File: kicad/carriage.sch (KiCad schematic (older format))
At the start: 21 parts, among them P10 \"1791-ZL262-8SG\", P11 \"1791-ZL262-8SG\", P12 \"1791-ZL262-8SG\", P13 \"1791-ZL262-8SG\", P8 \"1791-ZL262-8SG\", P9 \"1791-ZL262-8SG\", Q1 IRLR2905ZPBF, U1 \"1815-CD40109BPWR\"

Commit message: Draw schematic
Added sheet for panel connector and sheet for Y axis circuits.
Added ULN2803

References: #1 #11 #7 #5
Close #13
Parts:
- removed P10: \"1791-ZL262-8SG\", 7408hacks/dibfv, symbol "1791-ZL262-8SG"
- removed unit 3 of U1
- removed unit 4 of U1
- removed unit 5 of U1
- added C? (x2): 4u7/10V, 0805, symbol C
- added C?: \"1795-EEEFK1V101XP\", 7408hacks/dnxpf, symbol "1795-EEEFK1V101XP"
- added D? (x2): RED, 0805, symbol LED
- added JP?: \"1797-61300621121\", 7408hacks/dnxpn, symbol "1797-61300621121"
- added P9, P? (x2): \"1791-ZL262-8SG\", 7408hacks/dibfv, symbol "1791-ZL262-8SG"
- added Q2: IRLR2905ZPBF, D-PAK, symbol IRLR2905ZPBF
- added R7, R8, R? (x2): 22k, 0603, symbol R
- added R9: 10R, 0603, symbol R
- added R? (x4): 4k7 1%, 0603, symbol R
- added U?: \"1762-ULN2803ADW\", Plecharts/axkx7, symbol "1762-ULN2803ADW"
- R1, R2, R3, R4, R5, R6: value 10k -> 22k
- R10: renamed from R7; value 10k -> 10R
- renumbered P9 to P10
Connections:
- net labels added: A13, A14, A8, D46, D48, D9
- wire segments 96 -> 142
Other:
- note added: "Z"
- moved on the sheet: R10

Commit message: Draw schematic
Commit before trying newer version of KiCad
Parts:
- gave numbers to parts that had none: 15

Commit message: Draw schematic
Finished redrawing basic RAMPS schematic

References: #1 #4 #7 #15
Close #5 #17 #18
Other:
- note added: "Standard 40W heater @12V - 3.4A\n40W heater @24V - 1.7A"
- note added: "Standard IDC 2.54mm:\n- curent rating 2-3A\n- contact resistance max. 20mOhm\n\nStandard ribbon cable 1.27mm pitch, 28AWG (0.08mm2):\n- current rating 1A (dT=10*C)\n- resistance 0,24Ohm/m\n\nThere is also thicker 26AWG (0.13mm2) version.\n"
- moved on the sheet: R7, R8

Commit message: Change components to my own
References: #1 #19
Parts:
- removed C1, C2, C3, C8: \"1795-EEEFK1V101XP\", 7408hacks/dnxpf, symbol "1795-EEEFK1V101XP"
- removed C9: 4u7/10V, 0805, symbol C
- removed R1, R17, R18, R2, R4, R5: 22k, 0603, symbol R
- removed R21: 4k7 1%, 0603, symbol R
- added C7: 4u7/10V, 0805, symbol C
- added C? (x4): 100u/35V, symbol Cpol
- added R11: 4k7 1%, 0603, symbol R
- added R13: 10R, 0603, symbol R
- added R14, R15, R16, R3, R9: 22k, 0603, symbol R
- R10: value 10R -> 22k
- renumbered C10 to C4, D3 to D6, D2 to D7, JP2 to JP1, JP1 to JP2, JP5 to JP3, JP3 to JP4, P9 to P2, P11 to P3, P8 to P4, P10 to P5, P16 to P6, P17 to P7, P12 to P8, P13 to P9, R20 to R1, R19 to R12, R3 to R2, R22 to R4, R9 to R5
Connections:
- wire segments 142 -> 144
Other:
- moved on the sheet: C4, R1, R12, R2, R4, R5

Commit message: Add YZ connector. Add endstop filters.
Close #23
References: #3 #20
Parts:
- removed C? (x3): 100u/35V, symbol Cpol
- removed JP1, JP2, JP3, JP4: \"1797-61300621121\", 7408hacks/dnxpn, symbol "1797-61300621121"
- removed P2, P3, P4, P5, P6, P7, P8, P9: \"1791-ZL262-8SG\", 7408hacks/dibfv, symbol "1791-ZL262-8SG"
- removed R10, R14, R3, R8, R9: 22k, 0603, symbol R
- removed R12: 4k7 1%, 0603, symbol R
- removed U1: \"1815-CD40109BPWR\", 7408hacks/doacj, symbol "1815-CD40109BPWR"
- removed U2: \"1762-ULN2803ADW\", Plecharts/axkx7, symbol "1762-ULN2803ADW"
- added C10, C9: 100n/50V, 0603, symbol C
- added C? (x2): 100u/35V, symbol Cpol
- added CON10, CON? (x2): Stepstick_Right_Connector, symbol Stepstick_Right_Connector
- added CON13: Carriage, IDC34, symbol CON17x2
- added CON9, CON? (x2): Stepstick_Left_Connector, symbol Stepstick_Left_Connector
- added JP1, JP? (x2): Jumper3, symbol Jumper3
- added R13, R? (x4): 22k, 0603, symbol R
- added R?: 4k7 1%, 0603, symbol R
- added U1: CD40109BPWR, TSSOP16, symbol CD40109BPWR
- added U2: ULN2803ADW, SO18, symbol ULN2803ADW
- Q1, Q2: footprint D-PAK -> DPAK3
- R15, R16: value 22k -> 4k7 1%
- gave numbers to parts that had none: 1
- renumbered R13 to R12
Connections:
- net labels added: D11, D2, D3, D4, D5, D6, D?, E1MotorA, E1MotorB, E1MotorC, E1MotorD, E2MotorA, E2MotorB, E2MotorC, E2MotorD, IOREF, OC1, OC2, OC3, OC4, OC5, OC6, OC7, OC8, Therm1, Therm2, Vheat, Vmot, Xmax, Xmin, XmotorA, XmotorB, XmotorC, XmotorD, heater1, heater2
- net labels removed: A8, D46, D48, VCC
- wire segments 144 -> 216
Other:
- note added: "Bandwidth 340Hz"
- note added: "Standard IDC 2.54mm:\n- curent rating 2-3A\n- contact resistance max. 20mOhm\n\nStandard ribbon cable 1.27mm pitch, 28AWG (0.08mm2):\n- current rating 1A (dT=10*C)\n- resistance 0,24Ohm/m\n\nThere is also thicker 26AWG (0.13mm2) version.\n\nStandard 40W heater @12V - 3.4A\n40W heater @24V - 1.7A"
- note removed: "1A"
- note removed: "1B"
- note removed: "2A"
- note removed: "2B"
- note removed: "DIR"
- note removed: "EN"
- note removed: "GND"
- note removed: "MS1"
- note removed: "MS2"
- note removed: "MS3"
- note removed: "RST"
- note removed: "SLP"
- note removed: "STEP"
- note removed: "Standard 40W heater @12V - 3.4A\n40W heater @24V - 1.7A"
- note removed: "Standard IDC 2.54mm:\n- curent rating 2-3A\n- contact resistance max. 20mOhm\n\nStandard ribbon cable 1.27mm pitch, 28AWG (0.08mm2):\n- current rating 1A (dT=10*C)\n- resistance 0,24Ohm/m\n\nThere is also thicker 26AWG (0.13mm2) version.\n"
- note removed: "VDD"
- note removed: "Vmot"
- note removed: "Z"
- moved on the sheet: C4, C5, C7, D7, R12, R2, R4, R5, R6, R7

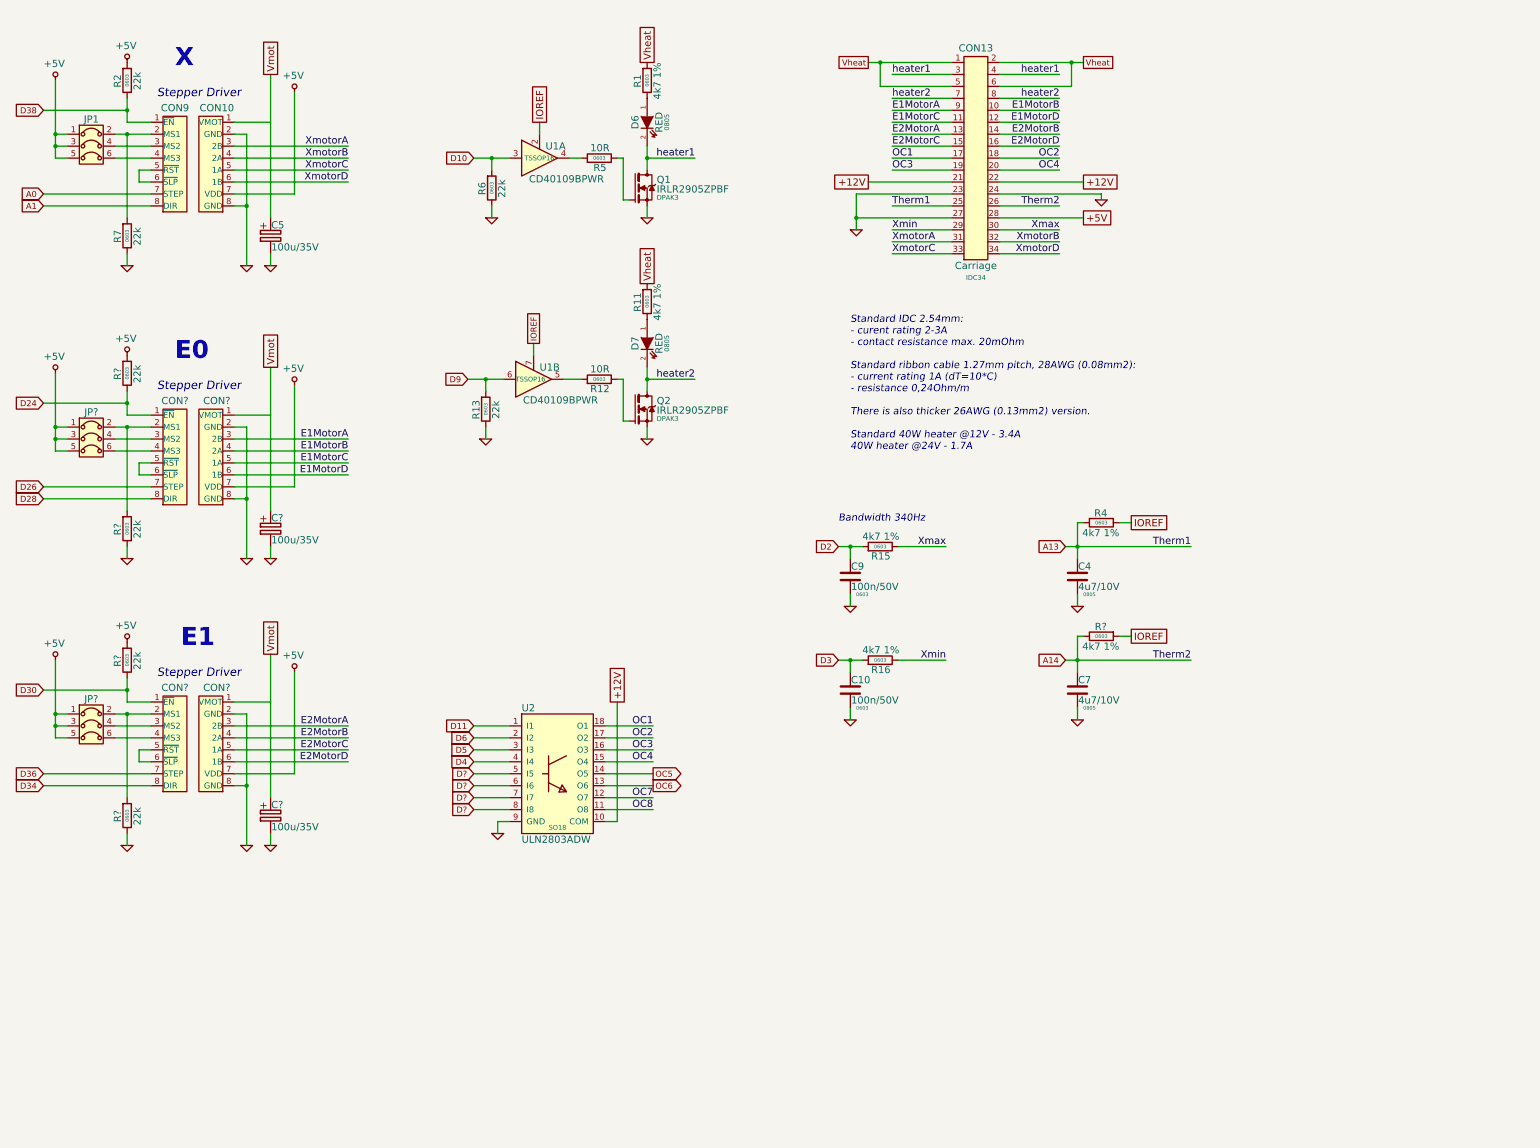
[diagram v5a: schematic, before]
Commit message: Add panel connectors. Minor ERC fixes.
References: #11
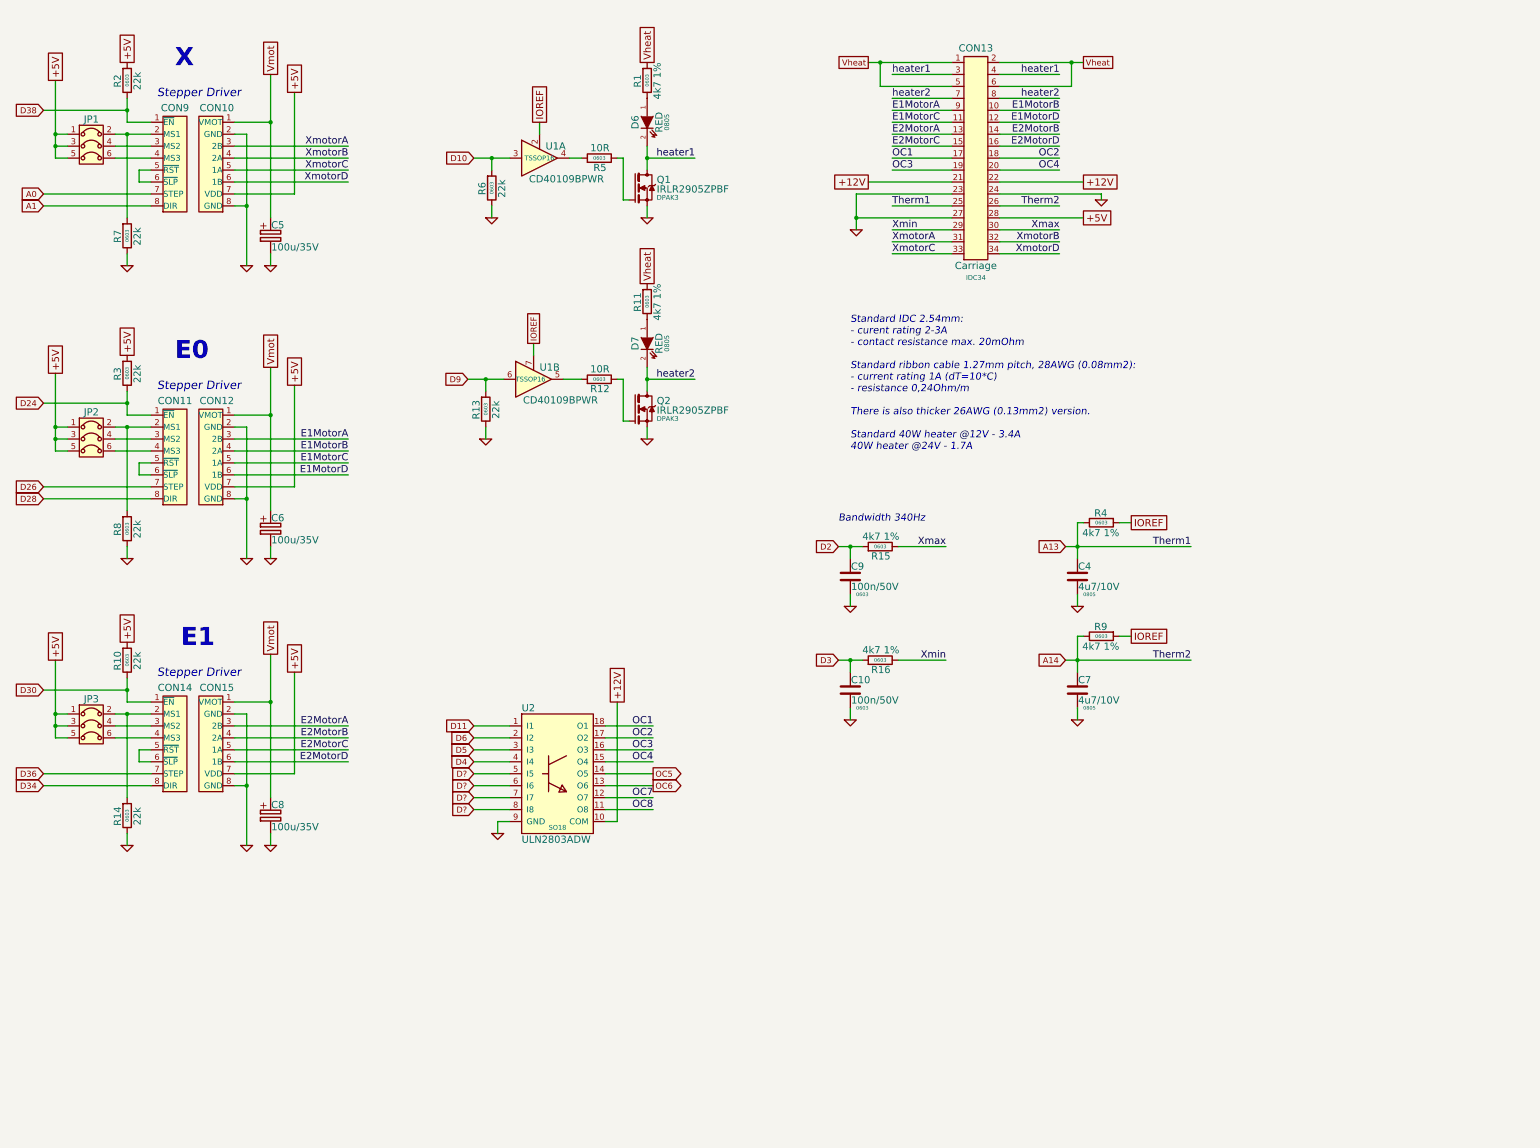
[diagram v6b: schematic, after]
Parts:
- gave numbers to parts that had none: 13
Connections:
- net Vmot: now also CON10.1 (VMOT), CON12.1 (VMOT), CON15.1 (VMOT)

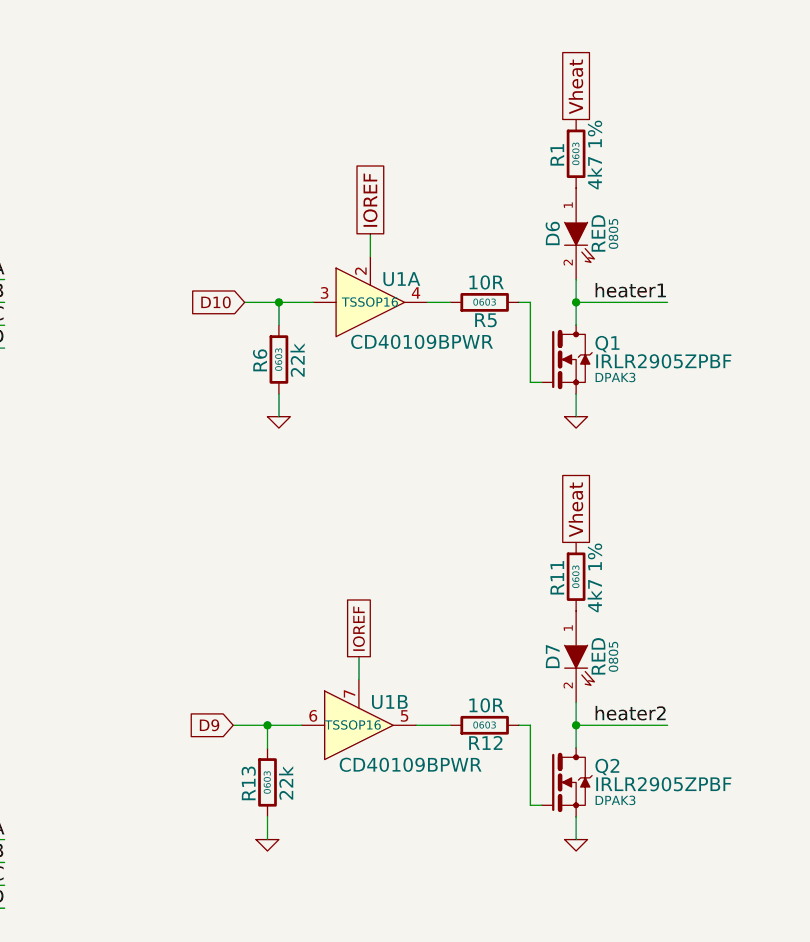
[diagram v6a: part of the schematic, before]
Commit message: Change CD40109 to CD4504
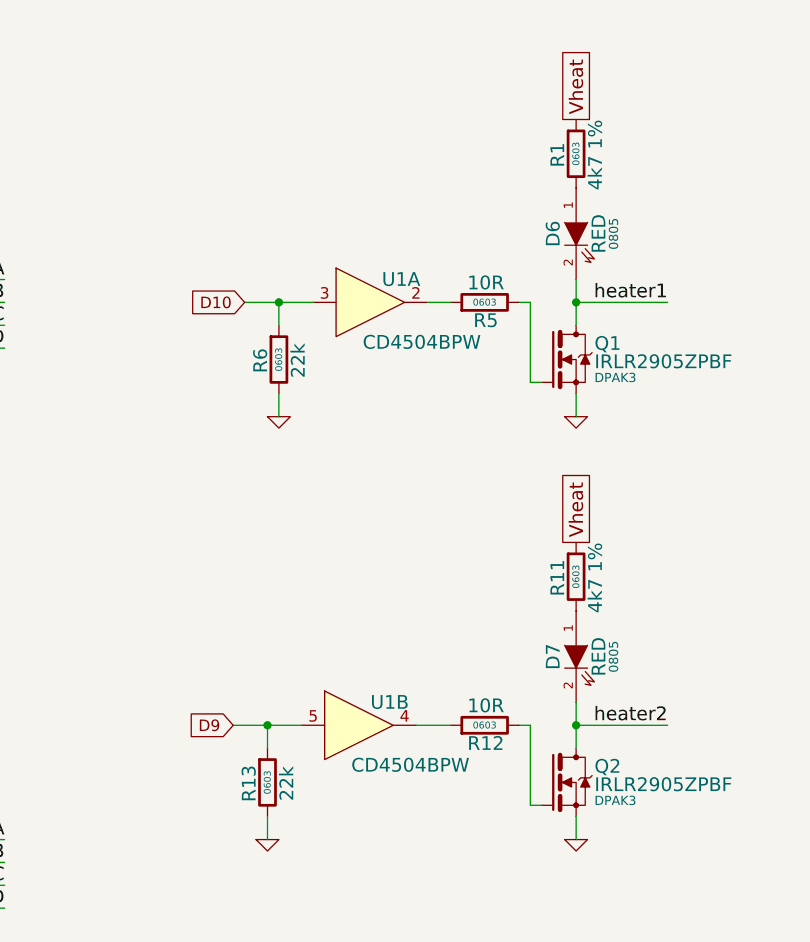
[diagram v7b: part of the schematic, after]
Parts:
- removed U1: CD40109BPWR, TSSOP16, symbol CD40109BPWR
- added U1: CD4504BPW, TSSOP16, symbol CD4504BPW
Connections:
- net D10: now also U1.3 (IN1)
- net D9: now also U1.5 (IN2)
- net at R5.1: now also U1.2 (OUT1)
- net at R12.1: now also U1.4 (OUT2)
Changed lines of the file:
@@
 A1
 $Comp
-L GND #PWR018
+L GND #PWR17
 U 1 1 534EC79B
 P 2700 2500
-F 0 "#PWR018" H 2700 2500 30  0001 C CNN
+F 0 "#PWR17" H 2700 2500 30  0001 C CNN
 F 1 "GND" H 2700 2430 30  0001 C CNN
 F 2 "~" H 2700 2500 60  0000 C CNN
@@
 $EndComp
 $Comp
-L GND #PWR019
+L GND #PWR16
 U 1 1 534EC7A1
 P 1700 2500
-F 0 "#PWR019" H 1700 2500 30  0001 C CNN
+F 0 "#PWR16" H 1700 2500 30  0001 C CNN
 F 1 "GND" H 1700 2430 30  0001 C CNN
 F 2 "~" H 1700 2500 60  0000 C CNN
@@
 D34
 $Comp
-L GND #PWR020
+L GND #PWR20
 U 1 1 534C44E8
 P 6050 3950
-F 0 "#PWR020" H 6050 3950 30  0001 C CNN
+F 0 "#PWR20" H 6050 3950 30  0001 C CNN
 F 1 "GND" H 6050 3880 30  0001 C CNN
 F 2 "~" H 6050 3950 60  0000 C CNN
@@
 D9
 $Comp
-L GND #PWR021
+L GND #PWR14
 U 1 1 534D96C2
 P 6050 2100
-F 0 "#PWR021" H 6050 2100 30  0001 C CNN
+F 0 "#PWR14" H 6050 2100 30  0001 C CNN
 F 1 "GND" H 6050 2030 30  0001 C CNN
 F 2 "~" H 6050 2100 60  0000 C CNN
@@
 D10
 $Comp
-L GND #PWR022
+L GND #PWR13
 U 1 1 534D96EE
 P 4750 2100
-F 0 "#PWR022" H 4750 2100 30  0001 C CNN
+F 0 "#PWR13" H 4750 2100 30  0001 C CNN
 F 1 "GND" H 4750 2030 30  0001 C CNN
 F 2 "~" H 4750 2100 60  0000 C CNN
@@
 $EndComp
 $Comp
-L GND #PWR023
+L GND #PWR25
 U 1 1 534EDD0C
 P 9650 5350
-F 0 "#PWR023" H 9650 5350 30  0001 C CNN
+F 0 "#PWR25" H 9650 5350 30  0001 C CNN
 F 1 "GND" H 9650 5280 30  0001 C CNN
 F 2 "~" H 9650 5350 60  0000 C CNN
@@
 A13
 $Comp
-L GND #PWR024
+L GND #PWR27
 U 1 1 534EDD2B
 P 9650 6300
-F 0 "#PWR024" H 9650 6300 30  0001 C CNN
+F 0 "#PWR27" H 9650 6300 30  0001 C CNN
 F 1 "GND" H 9650 6230 30  0001 C CNN
 F 2 "~" H 9650 6300 60  0000 C CNN
@@
 $EndComp
 $Comp
-L GND #PWR025
+L GND #PWR28
 U 1 1 534EDF1E
 P 4800 7250
-F 0 "#PWR025" H 4800 7250 30  0001 C CNN
+F 0 "#PWR28" H 4800 7250 30  0001 C CNN
 F 1 "GND" H 4800 7180 30  0001 C CNN
 F 2 "~" H 4800 7250 60  0000 C CNN
@@
 $EndComp
 $Comp
-L GND #PWR026
+L GND #PWR18
 U 1 1 536FB0A2
 P 2900 2500
-F 0 "#PWR026" H 2900 2500 30  0001 C CNN
+F 0 "#PWR18" H 2900 2500 30  0001 C CNN
 F 1 "GND" H 2900 2430 30  0001 C CNN
 F 2 "~" H 2900 2500 60  0000 C CNN
@@
 +12V
 $Comp
-L GND #PWR027
+L GND #PWR15
 U 1 1 536FC9C8
 P 7800 2200
-F 0 "#PWR027" H 7800 2200 30  0001 C CNN
+F 0 "#PWR15" H 7800 2200 30  0001 C CNN
 F 1 "GND" H 7800 2130 30  0001 C CNN
 F 2 "~" H 7800 2200 60  0000 C CNN
@@
 $EndComp
 $Comp
-L GND #PWR028
+L GND #PWR12
 U 1 1 536FC9D3
 P 9850 1950
-F 0 "#PWR028" H 9850 1950 30  0001 C CNN
+F 0 "#PWR12" H 9850 1950 30  0001 C CNN
 F 1 "GND" H 9850 1880 30  0001 C CNN
 F 2 "~" H 9850 1950 60  0000 C CNN
@@
 	1    0    0    -1
 $EndComp
-Text GLabel 5150 1300 1    60   UnSpc ~ 0
-IOREF
-$Comp
-L CD40109BPWR U1
-U 1 1 536FEAB2
-P 5150 1600
-F 0 "U1" H 5200 1700 60  0000 L CNN
-F 1 "CD40109BPWR" H 5375 1425 60  0000 C CNN
-F 2 "TSSOP16" H 5025 1600 40  0000 L CNN
-F 3 "" H 5000 2200 60  0001 L CNN
-	1    5150 1600
-	1    0    0    -1
-$EndComp
-$Comp
-L GND #PWR029
+$Comp
+L GND #PWR19
 U 1 1 536FECC5
 P 4700 3950
-F 0 "#PWR029" H 4700 3950 30  0001 C CNN
+F 0 "#PWR19" H 4700 3950 30  0001 C CNN
 F 1 "GND" H 4700 3880 30  0001 C CNN
 F 2 "~" H 4700 3950 60  0000 C CNN
@@
 F 3 "~" H 4700 3700 30  0000 C CNN
 	1    4700 3700
-	1    0    0    -1
-$EndComp
-Text GLabel 5100 3150 1    50   UnSpc ~ 0
-IOREF
-$Comp
-L CD40109BPWR U1
-U 2 1 536FECD5
-P 5100 3450
-F 0 "U1" H 5150 3550 60  0000 L CNN
-F 1 "CD40109BPWR" H 5325 3275 60  0000 C CNN
-F 2 "TSSOP16" H 4950 3450 40  0000 L CNN
-F 3 "" H 4950 4050 60  0001 L CNN
-	2    5100 3450
 	1    0    0    -1
 $EndComp
@@
 $EndComp
 $Comp
-L GND #PWR030
+L GND #PWR24
 U 1 1 537E69CA
 P 7750 5350
-F 0 "#PWR030" H 7750 5350 30  0001 C CNN
+F 0 "#PWR24" H 7750 5350 30  0001 C CNN
 F 1 "GND" H 7750 5280 30  0001 C CNN
 F 2 "~" H 7750 5350 60  0000 C CNN
@@
 $EndComp
 $Comp
-L GND #PWR031
+L GND #PWR26
 U 1 1 537E6A07
 P 7750 6300
-F 0 "#PWR031" H 7750 6300 30  0001 C CNN
+F 0 "#PWR26" H 7750 6300 30  0001 C CNN
 F 1 "GND" H 7750 6230 30  0001 C CNN
 F 2 "~" H 7750 6300 60  0000 C CNN
@@
 Stepper Driver
 $Comp
-L GND #PWR032
+L GND #PWR22
 U 1 1 537E82FE
 P 2700 4950
-F 0 "#PWR032" H 2700 4950 30  0001 C CNN
+F 0 "#PWR22" H 2700 4950 30  0001 C CNN
 F 1 "GND" H 2700 4880 30  0001 C CNN
 F 2 "~" H 2700 4950 60  0000 C CNN
@@
 $EndComp
 $Comp
-L GND #PWR033
+L GND #PWR21
 U 1 1 537E830F
 P 1700 4950
-F 0 "#PWR033" H 1700 4950 30  0001 C CNN
+F 0 "#PWR21" H 1700 4950 30  0001 C CNN
 F 1 "GND" H 1700 4880 30  0001 C CNN
 F 2 "~" H 1700 4950 60  0000 C CNN
@@
 $EndComp
 $Comp
-L GND #PWR034
+L GND #PWR23
 U 1 1 537E832F
 P 2900 4950
-F 0 "#PWR034" H 2900 4950 30  0001 C CNN
+F 0 "#PWR23" H 2900 4950 30  0001 C CNN
 F 1 "GND" H 2900 4880 30  0001 C CNN
 F 2 "~" H 2900 4950 60  0000 C CNN
@@
 Stepper Driver
 $Comp
-L GND #PWR035
+L GND #PWR30
 U 1 1 537E8370
 P 2700 7350
-F 0 "#PWR035" H 2700 7350 30  0001 C CNN
+F 0 "#PWR30" H 2700 7350 30  0001 C CNN
 F 1 "GND" H 2700 7280 30  0001 C CNN
 F 2 "~" H 2700 7350 60  0000 C CNN
@@
 $EndComp
 $Comp
-L GND #PWR036
+L GND #PWR29
 U 1 1 537E8381
 P 1700 7350
-F 0 "#PWR036" H 1700 7350 30  0001 C CNN
+F 0 "#PWR29" H 1700 7350 30  0001 C CNN
 F 1 "GND" H 1700 7280 30  0001 C CNN
 F 2 "~" H 1700 7350 60  0000 C CNN
@@
 $EndComp
 $Comp
-L GND #PWR037
+L GND #PWR31
 U 1 1 537E83A1
 P 2900 7350
-F 0 "#PWR037" H 2900 7350 30  0001 C CNN
+F 0 "#PWR31" H 2900 7350 30  0001 C CNN
 F 1 "GND" H 2900 7280 30  0001 C CNN
 F 2 "~" H 2900 7350 60  0000 C CNN
@@
 	6100 6650 5700 6650
 Wire Wire Line
-	5150 1300 5150 1400
-Wire Wire Line
 	5400 1600 5500 1600
 Wire Wire Line
@@
 	4700 3550 4700 3450
 Connection ~ 4700 3450
-Wire Wire Line
-	5100 3150 5100 3250
 Wire Wire Line
 	7650 4850 7850 4850
@@
 Text GLabel 3100 5900 1    60   UnSpc ~ 0
 +5V
+$Comp
+L CD4504BPW U1
+U 1 1 538D6475
+P 5150 1600
+F 0 "U1" H 5200 1700 60  0000 L CNN
+F 1 "CD4504BPW" H 5375 1425 60  0000 C CNN
+F 2 "TSSOP16" H 5025 1600 40  0001 L CNN
+F 3 "" H 5000 2200 60  0001 L CNN
+	1    5150 1600
+	1    0    0    -1
+$EndComp
+$Comp
+L CD4504BPW U1
+U 2 1 538D6511
+P 5100 3450
+F 0 "U1" H 5150 3550 60  0000 L CNN
+F 1 "CD4504BPW" H 5325 3275 60  0000 C CNN
+F 2 "TSSOP16" H 4975 3450 40  0001 L CNN
+F 3 "" H 4950 4050 60  0001 L CNN
+	2    5100 3450
+	1    0    0    -1
+$EndComp
 $EndSCHEMATC
